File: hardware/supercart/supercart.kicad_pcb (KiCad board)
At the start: 2 copper layers, 57.7 x 90 mm, 3 parts, among them J1 C64_EDGE_CONNECTOR_44, U1 ATF22V10C_SUPERCART, U2 AM29F080B_SO44

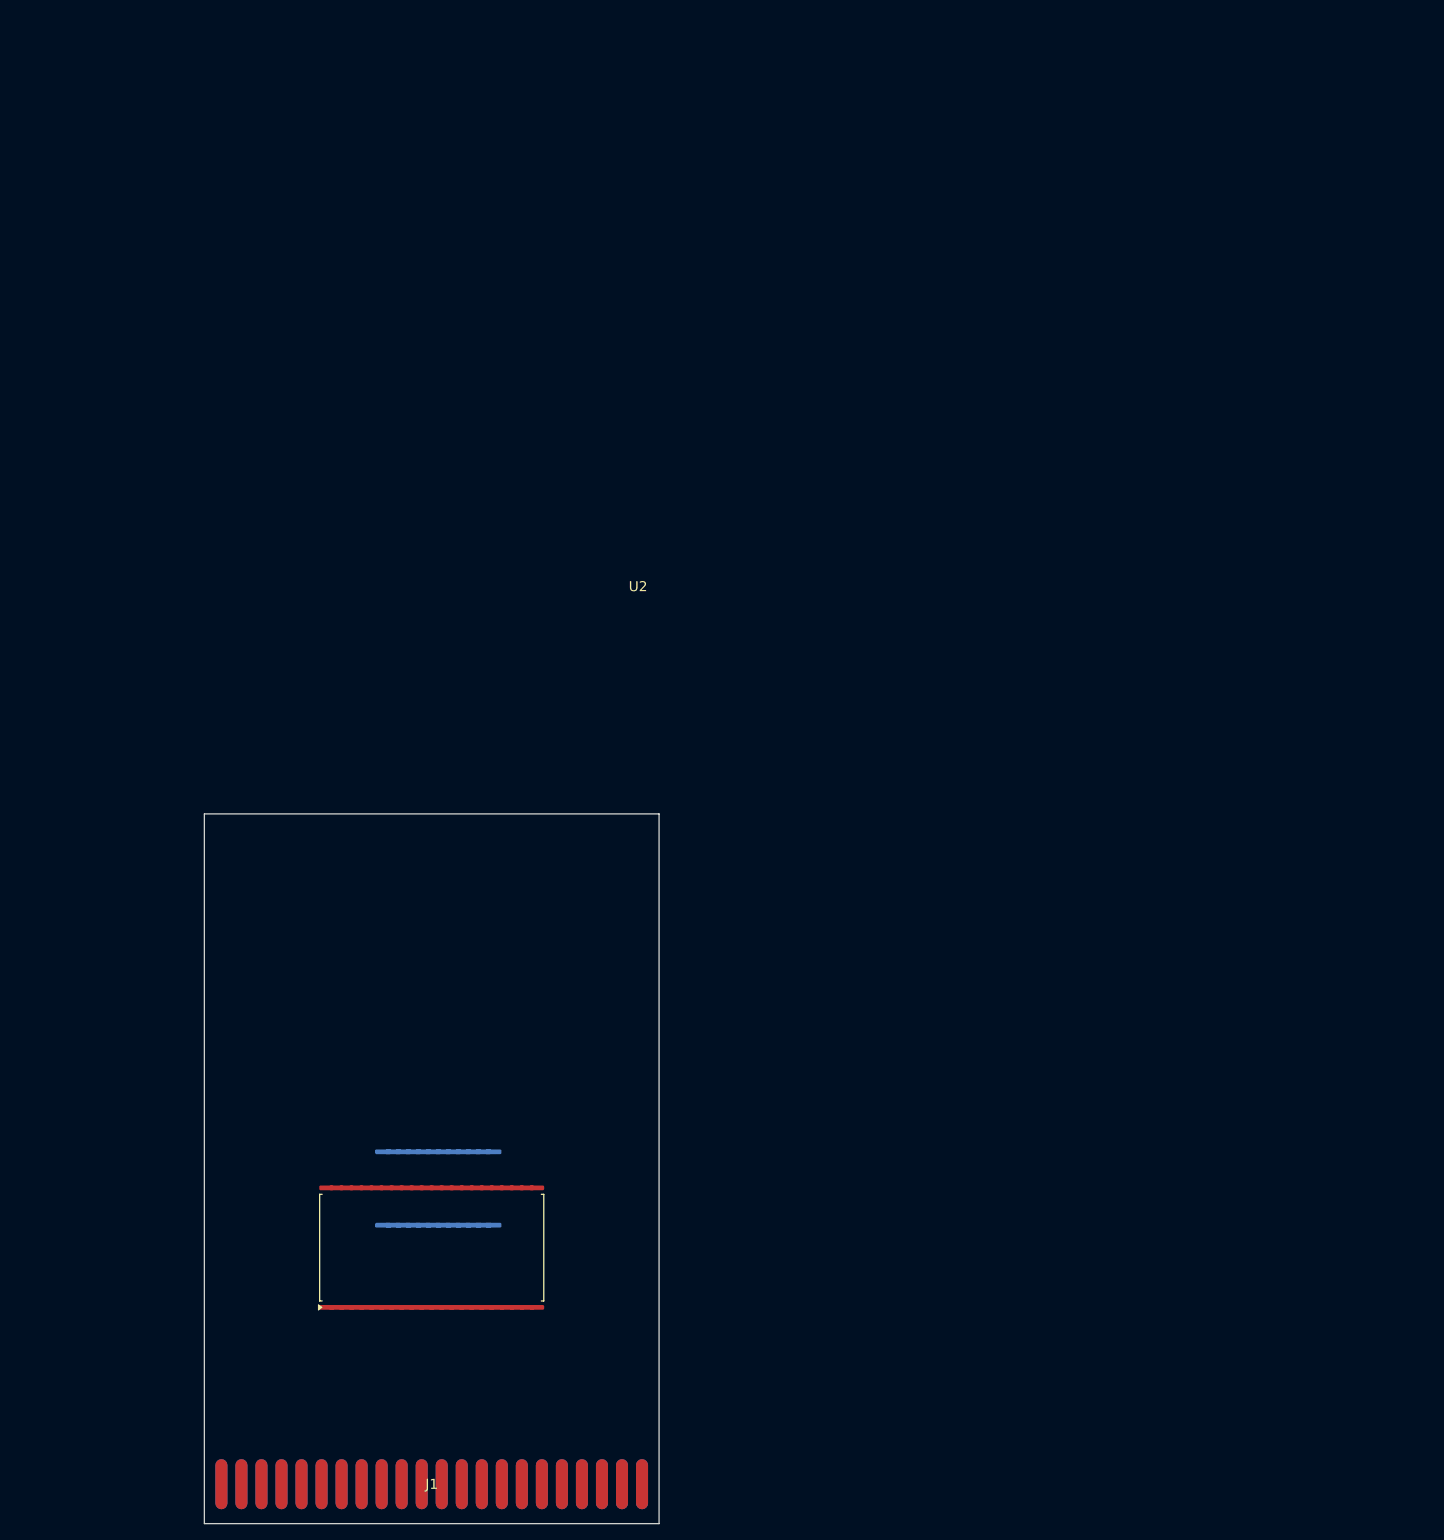
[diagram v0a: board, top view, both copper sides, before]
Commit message: Rework SuperCart layout to match a real reference board; add TestBoard
Cross-verified the whole design against hardware/TestBoard/EpyxFastLoad.kicad_pcb,
a real Epyx FastLoad cartridge reproduction that happened to be sitting in the
repo. Its connector footprint matched our c64-wiki-derived pinout on every
single pin, independently confirming it. Adopted several real details from it:

- Connector pads switched from oval (EasyFlash-derived) to rectangular
  1.5x9mm, matching EpyxFastLoad exactly
- Pins 3 and A tied to +5V/GND (were unconnected) per its real precedent
- Board outline traced exactly from its Edge.Cuts geometry: sharp top
  corners, two inward side notches, 45-degree chamfered connector corners
  (an earlier guess at "rounded corners" from a mirrored screenshot was wrong)
- Board width matched to its 58.0mm; height tightened to 60mm (its 37.9mm
  isn't physically reachable -- our AM29F080B body alone is 28.2mm, verified
  from its datasheet, vs. the small DIP EPROM that board actually uses)

Also: diagnosed and fixed a KiCad DRC false-positive (rotated roundrect SMD
pads triggered bogus adjacent-pin shorts -- fixed by keeping ICs unrotated),
added missing decoupling caps (C1/C2), fixed a placement bug where U2 wasn't
actually top-aligned with U1, and substituted a 3D model for the AM29F080B
footprint since KiCad's own library ships its 2D pads but no matching .step
file.

Co-Authored-By: Claude Sonnet 5 <noreply@anthropic.com>
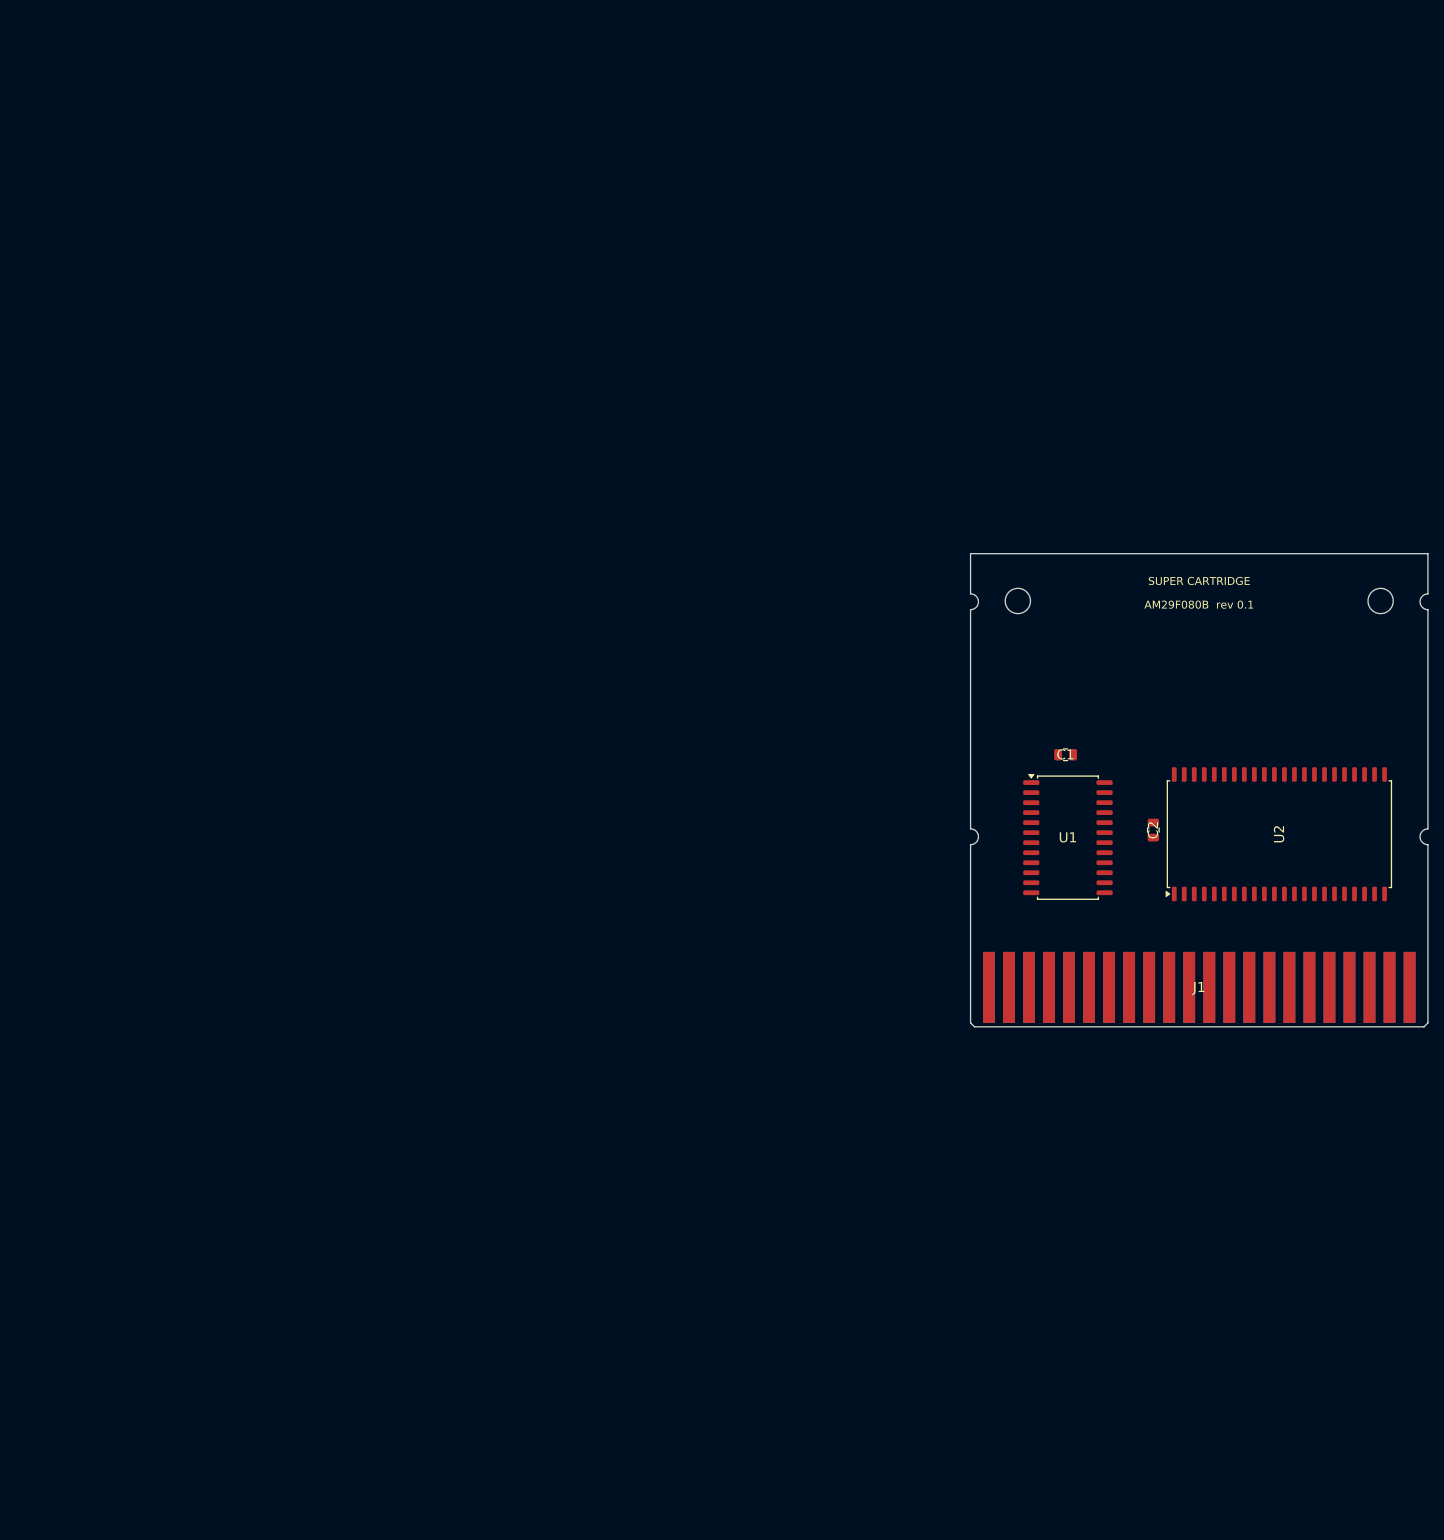
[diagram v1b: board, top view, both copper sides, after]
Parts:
- added ?: MountingHole_3.2mm_M3, MountingHole:MountingHole_3.2mm_M3, F.Cu at (127.0, 72.5)
- added ?: MountingHole_3.2mm_M3, MountingHole:MountingHole_3.2mm_M3, F.Cu at (173.0, 72.5)
- added C1: 0.1uF, Capacitor_SMD:C_0805_2012Metric, F.Cu at (133.1, 92.0)
- added C2: 0.1uF, Capacitor_SMD:C_0805_2012Metric, F.Cu at (144.2, 101.5)
- U1: moved to F.Cu
- moved U2 119.6 mm to (160.2, 102.1)
- moved J1 115.9 mm to (150.0, 121.5)
- moved U1 91.4 mm to (133.3, 102.5), turned to 0 degrees
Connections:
- net /A0 renamed A0
- net /A1 renamed A1
- net /A10 renamed A10
- net /A11 renamed A11
- net /A12 renamed A12
- net /A2 renamed A2
- net /A3 renamed A3
- net /A4 renamed A4
- net /A5 renamed A5
- net /A6 renamed A6
- net /A7 renamed A7
- net /A8 renamed A8
- net /A9 renamed A9
- net /BANK0 renamed BANK0
- net /BANK1 renamed BANK1
- net /BANK2 renamed BANK2
- net /BANK3 renamed BANK3
- net /BANK4 renamed BANK4
- net /BANK5 renamed BANK5
- net /BANK6 renamed BANK6
- net /D0 renamed D0
- net /D1 renamed D1
- net /D2 renamed D2
- net /D3 renamed D3
- net /D4 renamed D4
- net /D5 renamed D5
- net /D6 renamed D6
- net /D7 renamed D7
- net /IO1_N renamed IO1_N
- net /PHI2 renamed PHI2
- net /RESET_N renamed RESET_N
- net /RW renamed RW
- net /TBD_CTRL0 renamed TBD_CTRL0
- net /TBD_CTRL1_FLASH_WRITE_SAFETY renamed TBD_CTRL1_FLASH_WRITE_SAFETY
- net /TBD_CTRL2 renamed TBD_CTRL2
- net /TBD_EXROM_N renamed TBD_EXROM_N
- net /TBD_FLASH_CE_N renamed TBD_FLASH_CE_N
- net /TBD_FLASH_OE_N renamed TBD_FLASH_OE_N
- net /TBD_FLASH_RYBY_N renamed TBD_FLASH_RYBY_N
- net /TBD_FLASH_WE_N renamed TBD_FLASH_WE_N
- net /TBD_GAME_N renamed TBD_GAME_N
- net /TBD_ROMH_N renamed TBD_ROMH_N
- net /TBD_ROML_N renamed TBD_ROML_N
- J1 pad 1: /GND -> GND
- J1 pad 10: unconnected-(J1-IO2_N-Pad10) -> (no net)
- J1 pad 12: unconnected-(J1-BA-Pad12) -> (no net)
- J1 pad 13: unconnected-(J1-DMA_N-Pad13) -> (no net)
- J1 pad 2: /VCC -> VCC
- J1 pad 22: /GND -> GND
- J1 pad 3: unconnected-(J1-RESERVED_3-Pad3) -> VCC
- J1 pad 4: unconnected-(J1-IRQ_N-Pad4) -> (no net)
- J1 pad 6: unconnected-(J1-DOTCLK-Pad6) -> (no net)
- J1 pad A: unconnected-(J1-RESERVED_A-PadA) -> GND
- J1 pad D: unconnected-(J1-NMI_N-PadD) -> (no net)
- J1 pad F: unconnected-(J1-A15-PadF) -> (no net)
- J1 pad H: unconnected-(J1-A14-PadH) -> (no net)
- J1 pad J: unconnected-(J1-A13-PadJ) -> (no net)
- J1 pad Z: /GND -> GND
- U1 pad 12: /GND -> GND
- U1 pad 24: /VCC -> VCC
- U2 pad 1: unconnected-(U2-NC-Pad1) -> (no net)
- U2 pad 11: unconnected-(U2-NC-Pad11) -> (no net)
- U2 pad 12: unconnected-(U2-NC-Pad12) -> (no net)
- U2 pad 21: /GND -> GND
- U2 pad 22: /GND -> GND
- U2 pad 23: /VCC -> VCC
- U2 pad 31: unconnected-(U2-NC-Pad31) -> (no net)
- U2 pad 32: unconnected-(U2-NC-Pad32) -> (no net)
- U2 pad 33: unconnected-(U2-NC-Pad33) -> (no net)
- U2 pad 34: unconnected-(U2-NC-Pad34) -> (no net)
- U2 pad 44: /VCC -> VCC
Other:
- board size 57.7 x 90 mm -> 58 x 60 mm
- board text added: "AM29F080B rev 0.1"
- board text added: "SUPER CARTRIDGE"
- board text removed: "SUPER CARTRIDGE rev 0.1 - PLACEMENT NOT FINAL - connector F.Cu/B.Cu face assignment NOT verified vs a real cartridge, see project notes"
